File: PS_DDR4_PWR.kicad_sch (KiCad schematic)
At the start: 1 part, among them U12 K4A8G165WC-BCTD

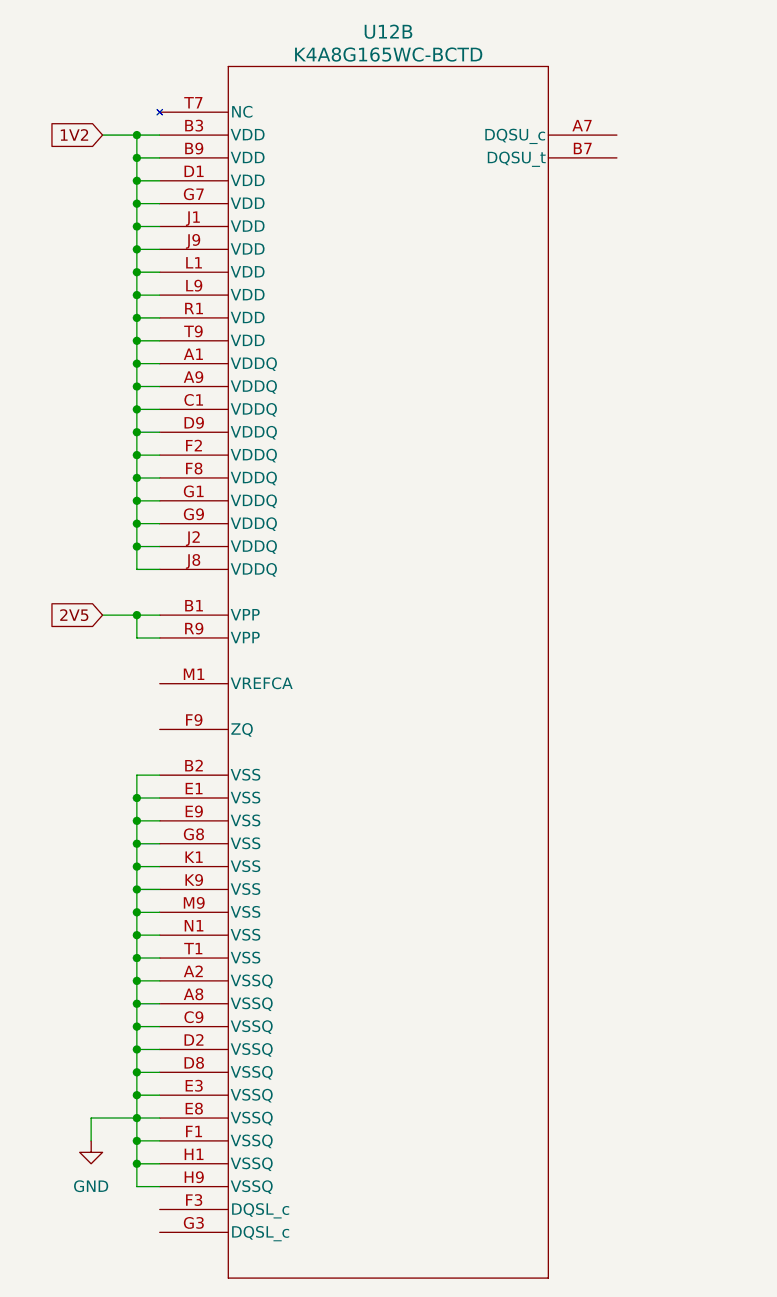
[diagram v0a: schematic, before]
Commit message: DDR4 added
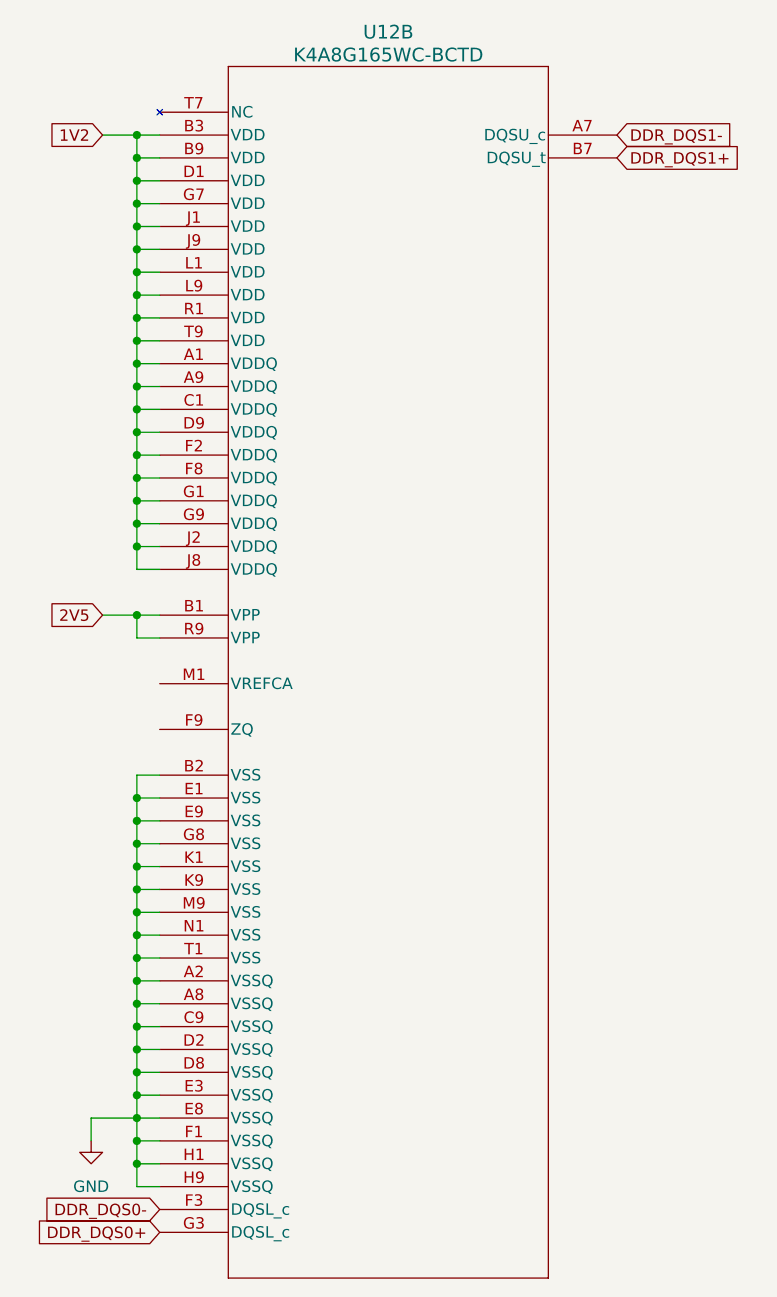
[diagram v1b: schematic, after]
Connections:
- net DDR_DQS1-: now reaches U12.A7 (DQSU_c)
- net DDR_DQS1+: now reaches U12.B7 (DQSU_t)
- net DDR_DQS0-: now reaches U12.F3 (DQSL_c)
- net DDR_DQS0+: now reaches U12.G3 (DQSL_c)
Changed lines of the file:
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@@
     (stroke (width 0) (type default))
+  )
+  (global_label "DDR_DQS1-" (shape input) (at 213.36 33.02 0) (fields_autoplaced)
+    (effects (font (size 1.27 1.27)) (justify left))
+    (property "Intersheetrefs" "${INTERSHEET_REFS}" (at 227.6353 33.02 0)
+      (effects (font (size 1.27 1.27)) (justify left) hide)
+    )
   )
   (global_label "2V5" (shape input) (at 156.21 86.36 180) (fields_autoplaced)
     (effects (font (size 1.27 1.27)) (justify right))
     (property "Intersheetrefs" "${INTERSHEET_REFS}" (at 149.7966 86.36 0)
+      (effects (font (size 1.27 1.27)) (justify right) hide)
+    )
+  )
+  (global_label "DDR_DQS0-" (shape input) (at 162.56 152.4 180) (fields_autoplaced)
+    (effects (font (size 1.27 1.27)) (justify right))
+    (property "Intersheetrefs" "${INTERSHEET_REFS}" (at 148.2847 152.4 0)
       (effects (font (size 1.27 1.27)) (justify right) hide)
     )
@@
       (effects (font (size 1.27 1.27)) (justify right) hide)
     )
+  )
+  (global_label "DDR_DQS1+" (shape input) (at 213.36 35.56 0) (fields_autoplaced)
+    (effects (font (size 1.27 1.27)) (justify left))
+    (property "Intersheetrefs" "${INTERSHEET_REFS}" (at 227.6353 35.56 0)
+      (effects (font (size 1.27 1.27)) (justify left) hide)
+    )
+  )
+  (global_label "DDR_DQS0+" (shape input) (at 162.56 154.94 180) (fields_autoplaced)
+    (effects (font (size 1.27 1.27)) (justify right))
+    (property "Intersheetrefs" "${INTERSHEET_REFS}" (at 148.2847 154.94 0)
+      (effects (font (size 1.27 1.27)) (justify right) hide)
+    )

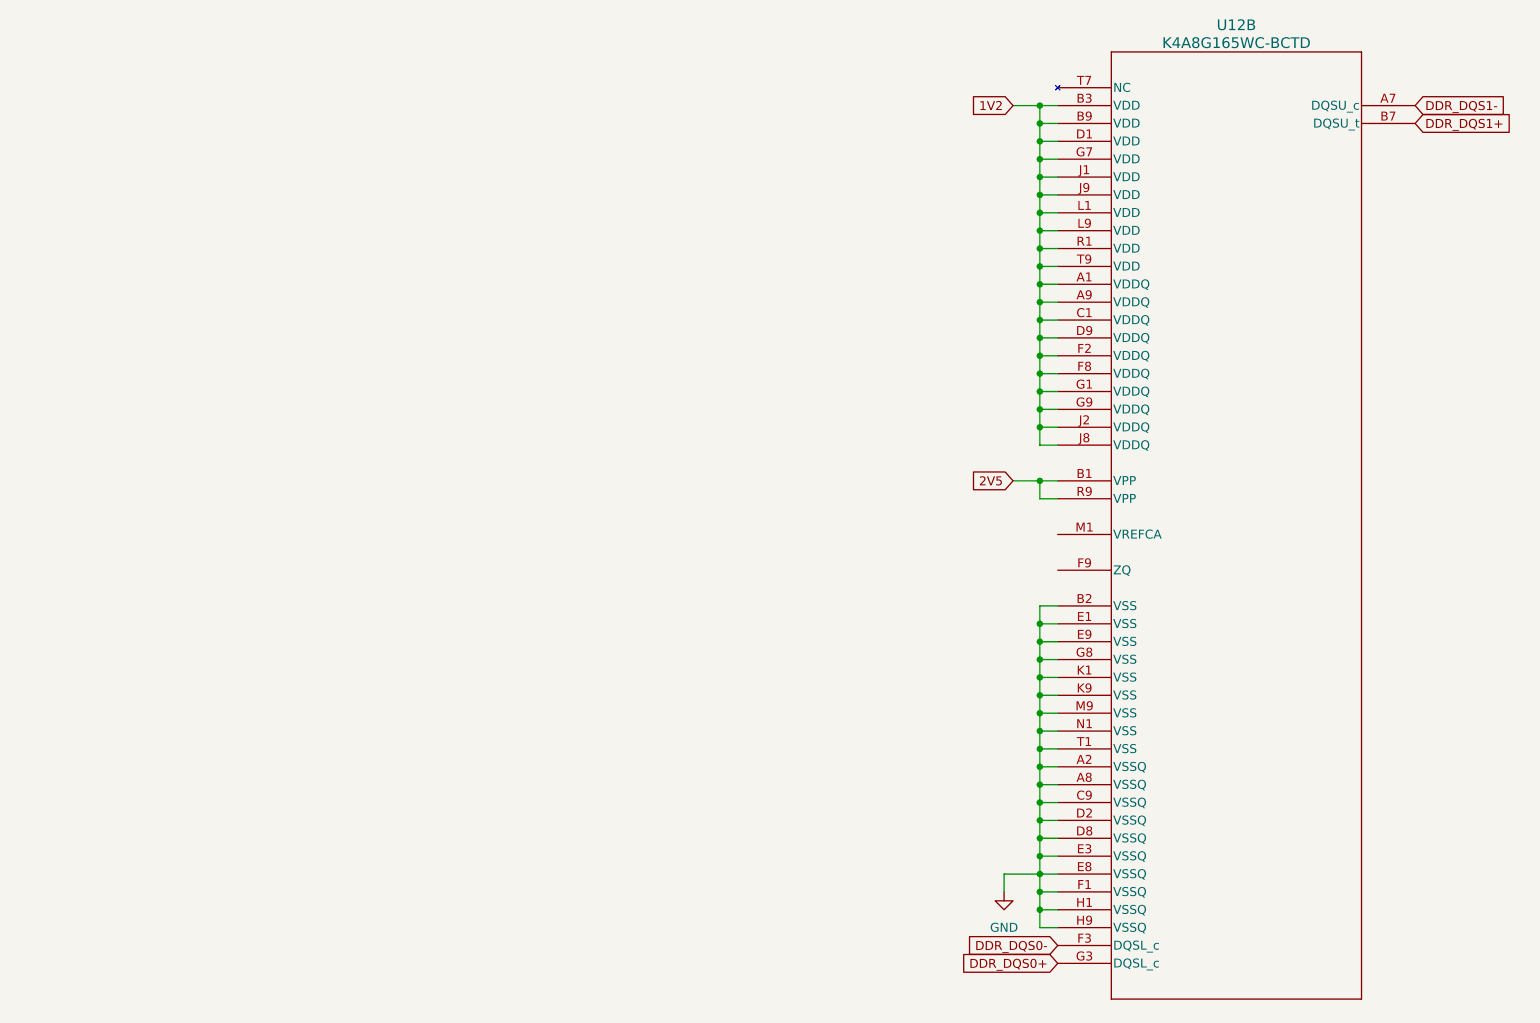
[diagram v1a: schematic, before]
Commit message: DDR4 data lines
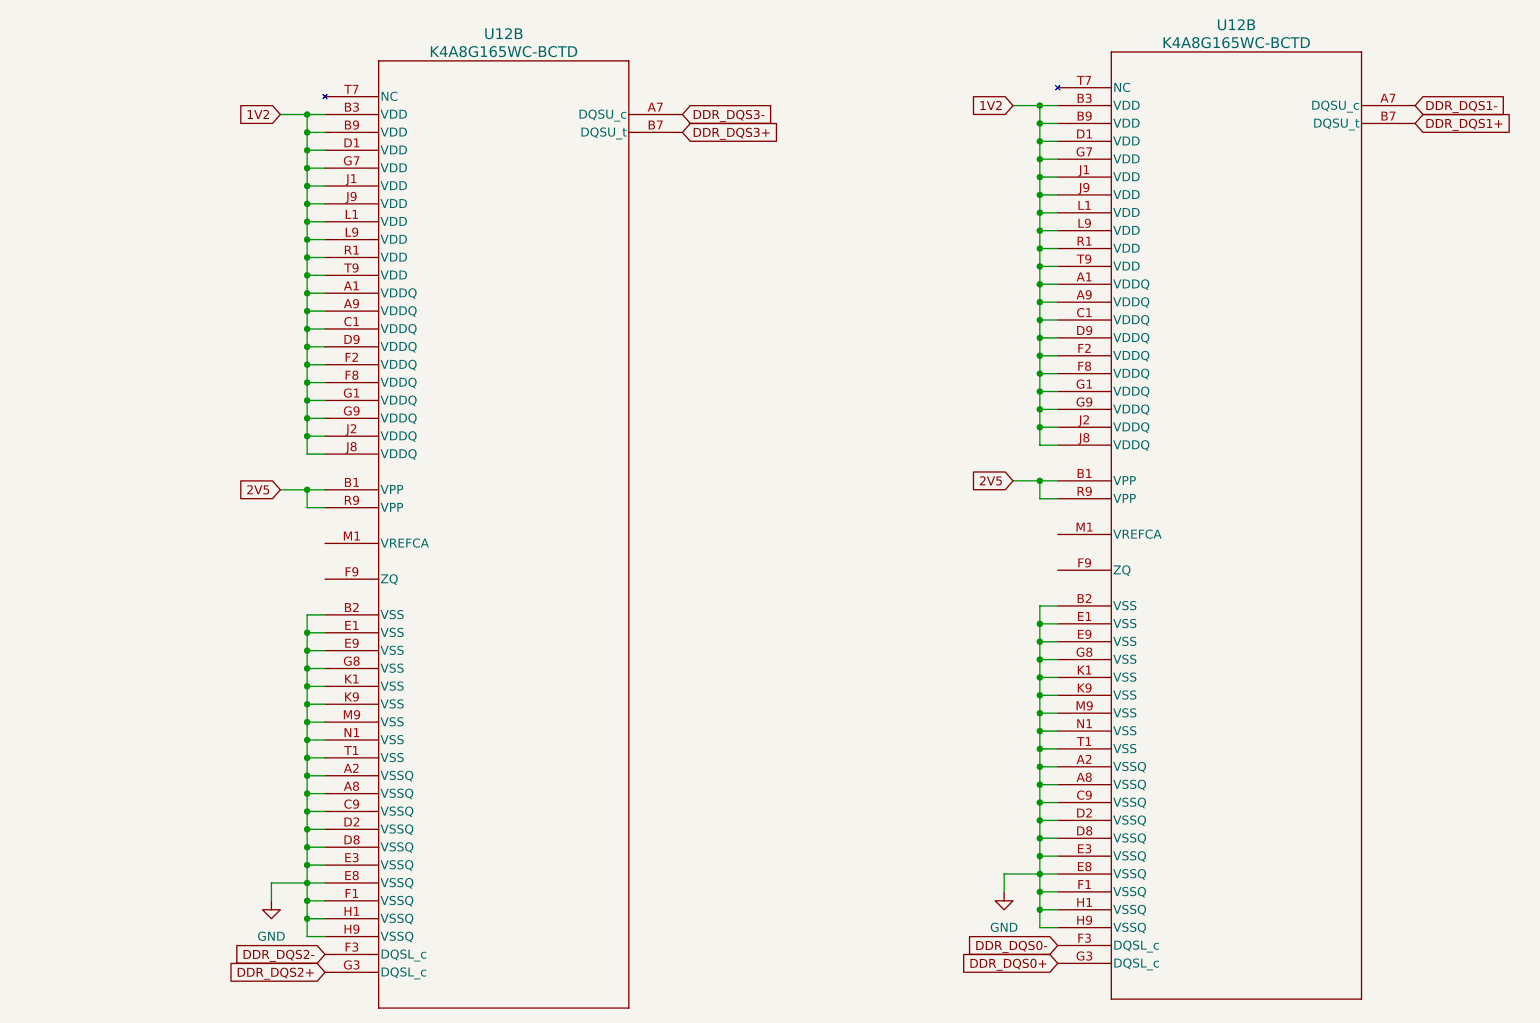
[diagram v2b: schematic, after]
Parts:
- added U12: K4A8G165WC-BCTD, lib:FBGA96X16_7P5X13P3_SAM, symbol K4A8G165W:K4A8G165WC-BCTD
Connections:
- net 1V2: now also U12.A1 (VDDQ), U12.A9 (VDDQ), U12.B3 (VDD), U12.B9 (VDD), U12.C1 (VDDQ), U12.D1 (VDD), U12.D9 (VDDQ), U12.F2 (VDDQ), U12.F8 (VDDQ), U12.G1 (VDDQ), U12.G7 (VDD), U12.G9 (VDDQ), U12.J1 (VDD), U12.J2 (VDDQ), U12.J8 (VDDQ), U12.J9 (VDD), U12.L1 (VDD), U12.L9 (VDD), U12.R1 (VDD), U12.T9 (VDD)
- net 2V5: now also U12.B1 (VPP), U12.R9 (VPP)
- net GND: now also U12.A2 (VSSQ), U12.A8 (VSSQ), U12.B2 (VSS), U12.C9 (VSSQ), U12.D2 (VSSQ), U12.D8 (VSSQ), U12.E1 (VSS), U12.E3 (VSSQ), U12.E8 (VSSQ), U12.E9 (VSS), U12.F1 (VSSQ), U12.G8 (VSS), U12.H1 (VSSQ), U12.H9 (VSSQ), U12.K1 (VSS), U12.K9 (VSS), U12.M9 (VSS), U12.N1 (VSS), U12.T1 (VSS)
- new net DDR_DQS2+: U12.G3 (DQSL_c)
- new net DDR_DQS2-: U12.F3 (DQSL_c)
- new net DDR_DQS3+: U12.B7 (DQSU_t)
- new net DDR_DQS3-: U12.A7 (DQSU_c)

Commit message: DDR4 finish
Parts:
- added C19, C20, C29, C30, C31, C32, C33, C34, C35, C38: 100nF, Capacitor_SMD:C_0402_1005Metric, symbol Device:C
- added C36, C37: 4.7uF, Capacitor_SMD:C_0603_1608Metric, symbol Device:C
- added R49, R50: 240, Resistor_SMD:R_0402_1005Metric, symbol Device:R
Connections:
- net 1V2: now also C19.1, C20.1, C29.1, C30.1, C31.1, C32.1, C33.1, C34.1
- net GND: now also C19.2, C20.2, C29.2, C30.2, C31.2, C32.2, C33.2, C34.2, C35.2, C36.2, C37.2, C38.2, R49.1, R50.1
- net at U12.F9 (ZQ): now also R50.2
- net DDR_VREF: now reaches U12.M1 (VREFCA)
- net DDR_VREF: now also U12.M1 (VREFCA)
- net at U12.F9 (ZQ): now also R49.2
- net 2V5 renamed 2V5_LDO
- net 2V5_LDO: now also C35.1, C36.1, C37.1, C38.1
